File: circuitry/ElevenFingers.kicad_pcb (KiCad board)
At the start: 2 copper layers, 3.6 x 3.6 mm, 95 parts, among them J1 OLED, SW1 MX, SW10 MX, SW11 MX, SW12 MX, SW13 MX, SW14 MX, SW15 MX, SW16 MX, SW17 MX, SW18 MX, SW19 MX, SW2 MX, SW20 MX, SW21 MX, SW22 MX, SW23 MX, SW24 MX, SW25 MX, SW26 MX, SW27 MX, SW28 MX, SW29 MX, SW3 MX, SW30 MX, SW4 MX, SW5 MX, SW6 MX, SW7 MX, SW8 MX, SW9 MX, U1 ProMicro, U2 TRRS

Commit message: keys all placed, 1 led placed, no tracing yet
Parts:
- moved D1 153.1 mm to (23.0, 58.0)
- moved L13 151.1 mm to (323.1, 117.0)
- moved D10 151.1 mm to (353.0, 53.0)
- moved D11 151.1 mm to (363.0, 53.0)
- moved D12 151.1 mm to (373.0, 53.0)
- moved D13 151.1 mm to (326.0, 61.0)
- moved D14 151.1 mm to (335.0, 61.0)
- moved D15 151.1 mm to (344.0, 61.0)
- moved D16 151.1 mm to (353.0, 61.0)
- moved D17 151.1 mm to (363.0, 61.0)
- moved D18 151.1 mm to (373.0, 61.0)
- moved D19 151.1 mm to (326.0, 70.0)
- moved D2 151.1 mm to (335.0, 45.0)
- moved D20 151.1 mm to (335.0, 70.0)
- moved D21 151.1 mm to (345.0, 70.0)
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
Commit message: started adding tracing
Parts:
- moved D19 296.7 mm to (38.1, 141.5), turned to 90 degrees
- moved D13 294.4 mm to (38.1, 122.5), turned to 90 degrees
- moved D7 292.3 mm to (38.1, 103.5), turned to 90 degrees
- moved D20 285.8 mm to (57.1, 136.7), turned to 90 degrees
- moved L13 285.1 mm to (38.1, 111.8)
- moved L7 285.0 mm to (38.1, 92.8)
- moved L19 285.0 mm to (38.1, 130.8)
- moved D14 283.7 mm to (57.1, 117.7), turned to 90 degrees
- moved D8 281.7 mm to (57.1, 98.7), turned to 90 degrees
- moved D2 280.1 mm to (57.1, 79.7), turned to 90 degrees
- moved L2 277.3 mm to (57.1, 69.0)
- moved L8 276.6 mm to (57.1, 88.0)
- moved L14 276.1 mm to (57.1, 107.0)
- moved L20 275.9 mm to (57.1, 126.0)
- moved D21 274.9 mm to (76.1, 127.2), turned to 90 degrees
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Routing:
- net GND: track 0.00 -> 73.4 mm
- net col3: track 0.00 -> 55.8 mm
- net col5: track 0.00 -> 55.8 mm
- net col1: track 0.00 -> 55.1 mm
- net col0: track 0.00 -> 55.1 mm
- net col2: track 0.00 -> 55.1 mm
- net col4: track 0.00 -> 55.1 mm
- net Net-(J1-Pad1): track 0.00 -> 28.5 mm
- net VCC: track 0.00 -> 26.6 mm
- net SERIAL: track 0.00 -> 26.1 mm
- net Net-(J1-Pad2): track 0.00 -> 23.1 mm
- net Net-(B1-Pad1): track 0.00 -> 22.2 mm
- net LED: track 0.00 -> 17.0 mm
- net unconnected-(U1-Pad20): track 0.00 -> 14.4 mm
- net row4: track 0.00 -> 14.4 mm
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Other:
- board size 3.6 x 3.6 mm -> 5.1 x 5.1 mm

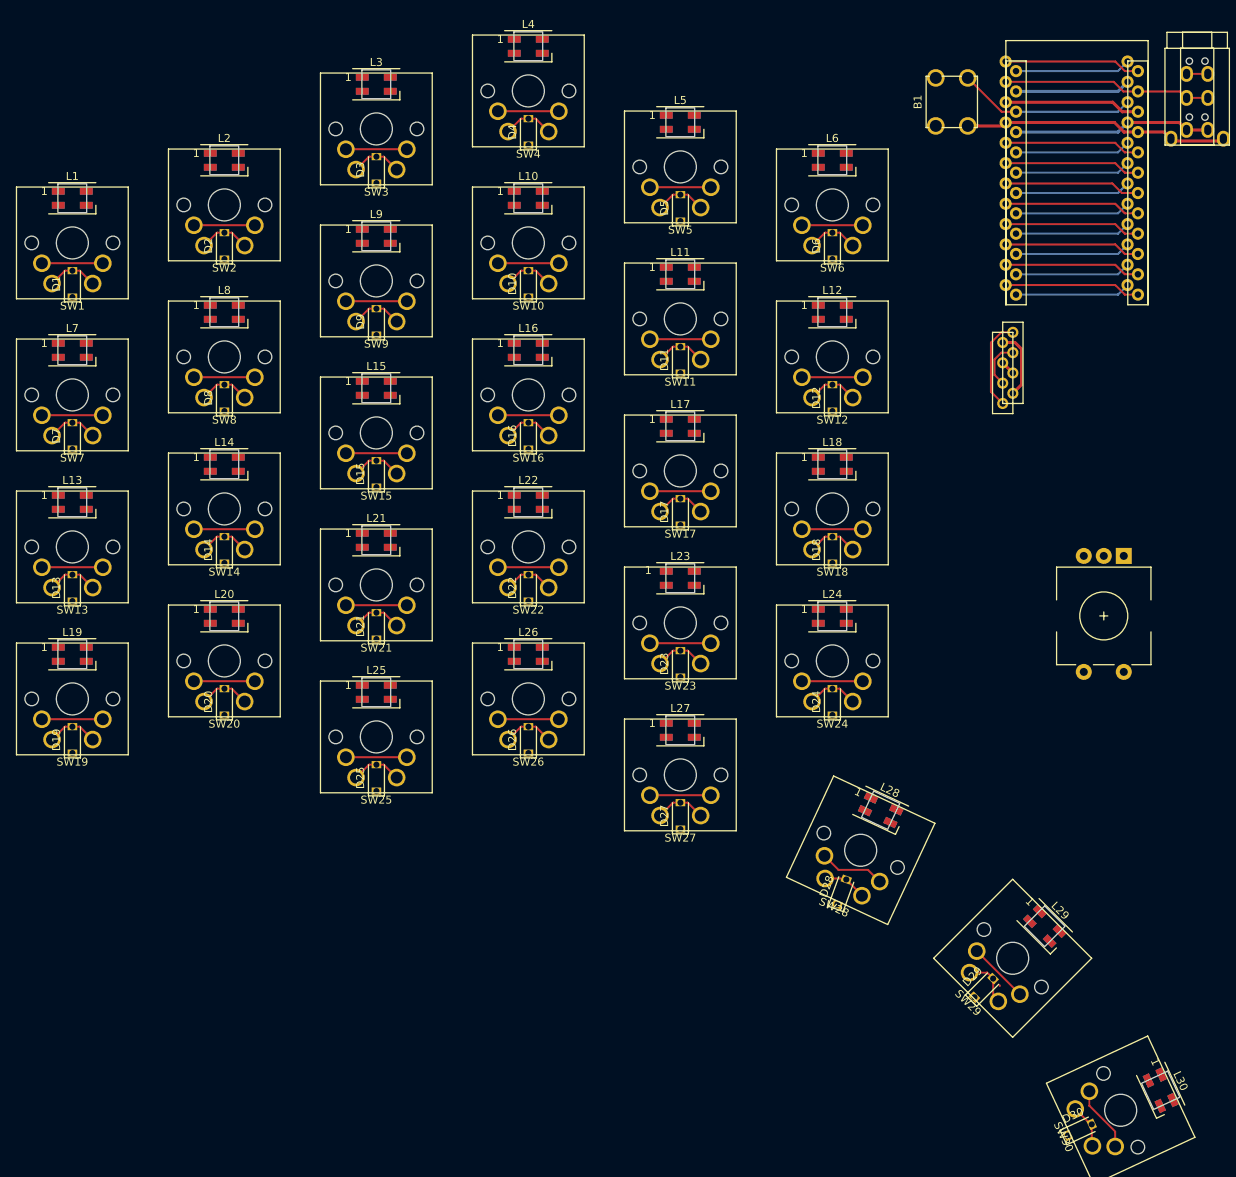
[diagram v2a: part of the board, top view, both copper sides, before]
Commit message: all components traced internally, not yet connected
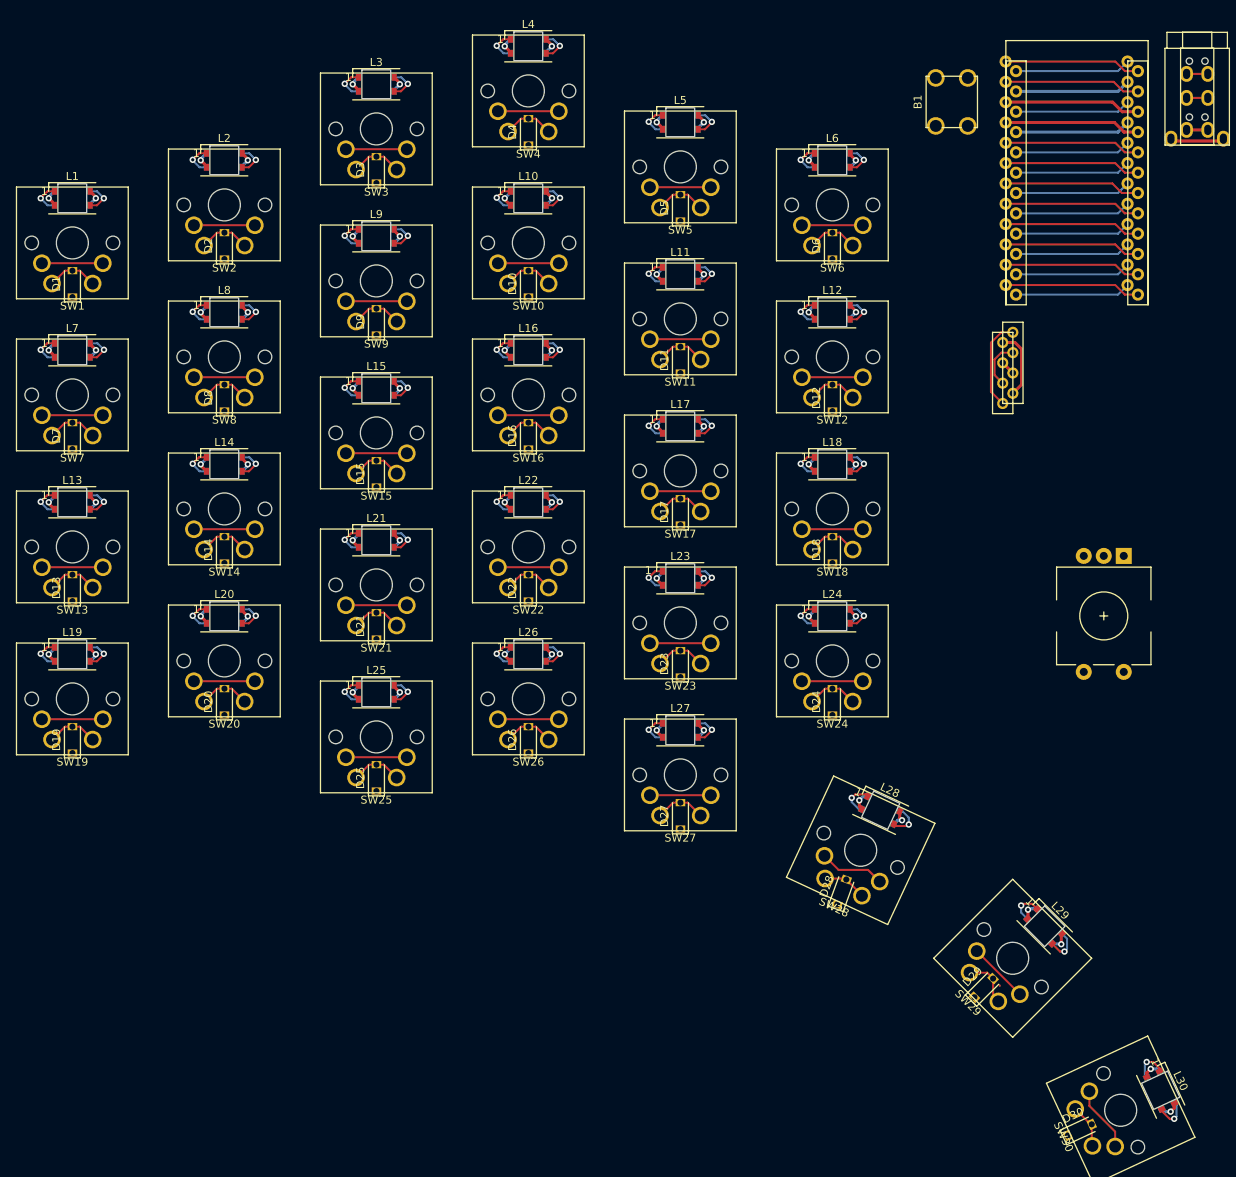
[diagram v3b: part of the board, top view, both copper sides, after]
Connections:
- L1 pad 4: LED -> Net-(L1-Pad4)
- L11 pad 2: Net-(L10-Pad4) -> Net-(L11-Pad2)
- L11 pad 4: Net-(L11-Pad4) -> Net-(L10-Pad2)
- L12 pad 2: Net-(L11-Pad4) -> Net-(L12-Pad2)
- L12 pad 4: Net-(L12-Pad4) -> Net-(L11-Pad2)
- L14 pad 2: Net-(L14-Pad2) -> Net-(L13-Pad4)
- L14 pad 4: Net-(L13-Pad2) -> Net-(L14-Pad4)
- L15 pad 2: Net-(L15-Pad2) -> Net-(L14-Pad4)
- L15 pad 4: Net-(L14-Pad2) -> Net-(L15-Pad4)
- L16 pad 2: Net-(L16-Pad2) -> Net-(L15-Pad4)
- L16 pad 4: Net-(L15-Pad2) -> Net-(L16-Pad4)
- L17 pad 2: Net-(L17-Pad2) -> Net-(L16-Pad4)
- L17 pad 4: Net-(L16-Pad2) -> Net-(L17-Pad4)
- L18 pad 2: Net-(L18-Pad2) -> Net-(L17-Pad4)
- L18 pad 4: Net-(L17-Pad2) -> Net-(L12-Pad2)
- L19 pad 4: Net-(L19-Pad4) -> Net-(L13-Pad2)
- L2 pad 2: Net-(L2-Pad2) -> Net-(L1-Pad4)
- L2 pad 4: Net-(L1-Pad2) -> Net-(L2-Pad4)
- L20 pad 2: Net-(L19-Pad4) -> Net-(L20-Pad2)
- L20 pad 4: Net-(L20-Pad4) -> Net-(L19-Pad2)
- L21 pad 2: Net-(L20-Pad4) -> Net-(L21-Pad2)
- L21 pad 4: Net-(L21-Pad4) -> Net-(L20-Pad2)
- L22 pad 2: Net-(L21-Pad4) -> Net-(L22-Pad2)
- L22 pad 4: Net-(L22-Pad4) -> Net-(L21-Pad2)
- L23 pad 2: Net-(L22-Pad4) -> Net-(L23-Pad2)
- L23 pad 4: Net-(L23-Pad4) -> Net-(L22-Pad2)
- L24 pad 2: Net-(L23-Pad4) -> Net-(L24-Pad2)
- L24 pad 4: Net-(L18-Pad2) -> Net-(L23-Pad2)
- L25 pad 2: Net-(L25-Pad2) -> unconnected-(L25-Pad2)
- L25 pad 4: Net-(L19-Pad2) -> Net-(L25-Pad4)
- L26 pad 2: Net-(L26-Pad2) -> Net-(L25-Pad4)
- L26 pad 4: Net-(L25-Pad2) -> Net-(L26-Pad4)
- L27 pad 2: Net-(L27-Pad2) -> Net-(L26-Pad4)
- L27 pad 4: Net-(L26-Pad2) -> Net-(L27-Pad4)
- L28 pad 2: Net-(L28-Pad2) -> Net-(L27-Pad4)
- L28 pad 4: Net-(L27-Pad2) -> Net-(L28-Pad4)
- L29 pad 2: Net-(L29-Pad2) -> Net-(L28-Pad4)
- L29 pad 4: Net-(L28-Pad2) -> Net-(L29-Pad4)
- L3 pad 2: Net-(L3-Pad2) -> Net-(L2-Pad4)
- L3 pad 4: Net-(L2-Pad2) -> Net-(L3-Pad4)
- L30 pad 2: unconnected-(L30-Pad2) -> Net-(L29-Pad4)
- L30 pad 4: Net-(L29-Pad2) -> Net-(L24-Pad2)
- L4 pad 2: Net-(L4-Pad2) -> Net-(L3-Pad4)
- L4 pad 4: Net-(L3-Pad2) -> Net-(L4-Pad4)
- L5 pad 2: Net-(L5-Pad2) -> Net-(L4-Pad4)
- L5 pad 4: Net-(L4-Pad2) -> Net-(L5-Pad4)
- L6 pad 2: Net-(L12-Pad4) -> Net-(L5-Pad4)
- L6 pad 4: Net-(L5-Pad2) -> LED
- L7 pad 2: Net-(L13-Pad4) -> Net-(L7-Pad2)
- L7 pad 4: Net-(L7-Pad4) -> Net-(L1-Pad2)
- L8 pad 2: Net-(L7-Pad4) -> Net-(L8-Pad2)
- L8 pad 4: Net-(L8-Pad4) -> Net-(L7-Pad2)
- L9 pad 2: Net-(L8-Pad4) -> Net-(L10-Pad4)
- L9 pad 4: Net-(L10-Pad2) -> Net-(L8-Pad2)
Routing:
- net VCC: track 26.6 -> 89.5 mm, vias 0 -> 30
- net GND: track 73.4 -> 135.4 mm, vias 0 -> 30
- net Net-(L29-Pad4): track 0.00 -> 8.87 mm, vias 0 -> 2
- net Net-(L28-Pad4): track 0.00 -> 8.63 mm, vias 0 -> 2
- net Net-(L27-Pad4): track 0.00 -> 8.60 mm, vias 0 -> 2
- net Net-(L24-Pad2): track 0.00 -> 8.51 mm, vias 0 -> 2
- net Net-(L10-Pad4): track 0.00 -> 8.46 mm, vias 0 -> 2
- net Net-(L11-Pad2): track 0.00 -> 8.46 mm, vias 0 -> 2
- net Net-(L10-Pad2): track 0.00 -> 8.44 mm, vias 0 -> 2
- net Net-(L23-Pad2): track 0.00 -> 8.44 mm, vias 0 -> 2
- net Net-(L13-Pad4): track 0.00 -> 8.44 mm, vias 0 -> 2
- net Net-(L1-Pad2): track 0.00 -> 8.44 mm, vias 0 -> 2
- net Net-(L12-Pad2): track 0.00 -> 8.44 mm, vias 0 -> 2
- net Net-(L8-Pad2): track 0.00 -> 8.44 mm, vias 0 -> 2
- net Net-(L26-Pad4): track 0.00 -> 8.44 mm, vias 0 -> 2
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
